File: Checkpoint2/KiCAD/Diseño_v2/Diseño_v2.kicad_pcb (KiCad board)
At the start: 2 copper layers, 160 x 125 mm, 41 parts, among them J1 Conn_01x02, J2 Conn_01x02, J3 Conn_01x03, Q1 BC547, Q2 BC547, Q3 BC557, Q4 BC557, Q5 BC547, Q6 TIP32A, Q7 BC547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

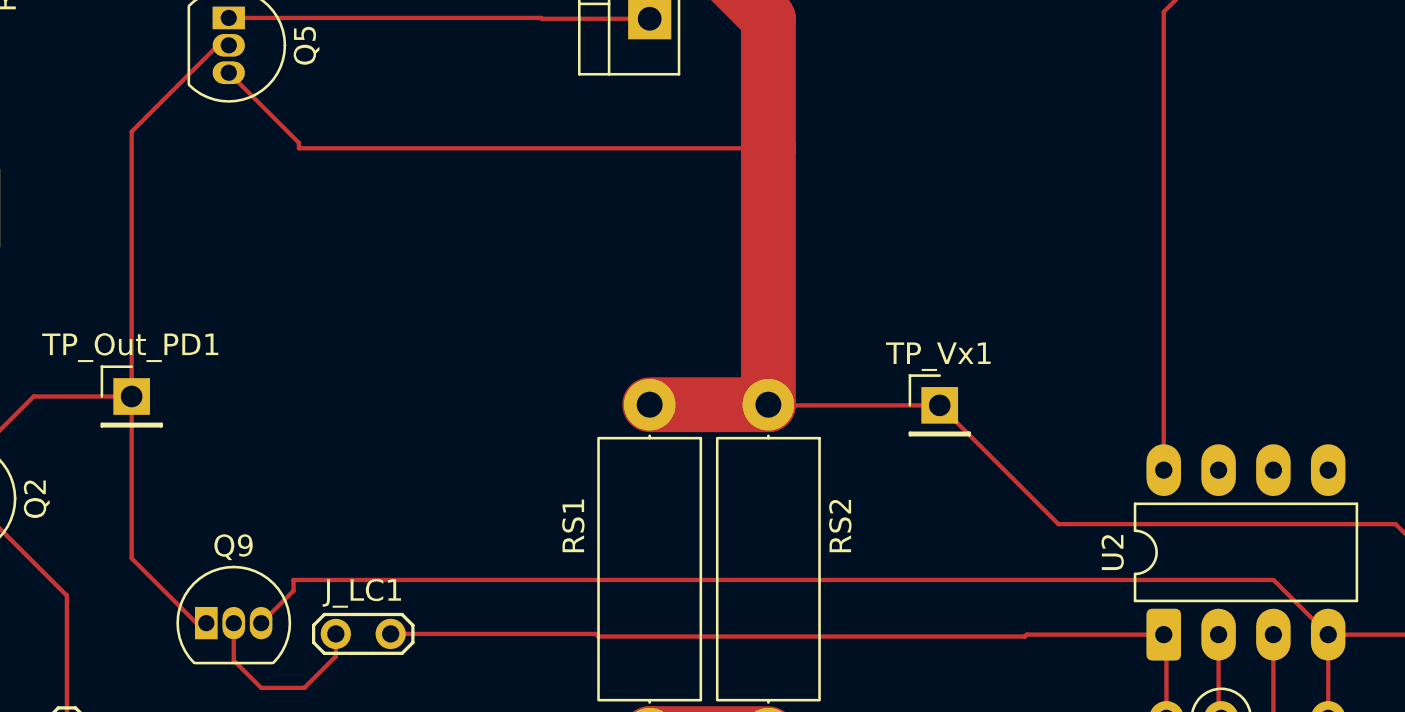
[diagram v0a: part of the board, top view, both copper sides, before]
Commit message: agregué el capacitor de compensación
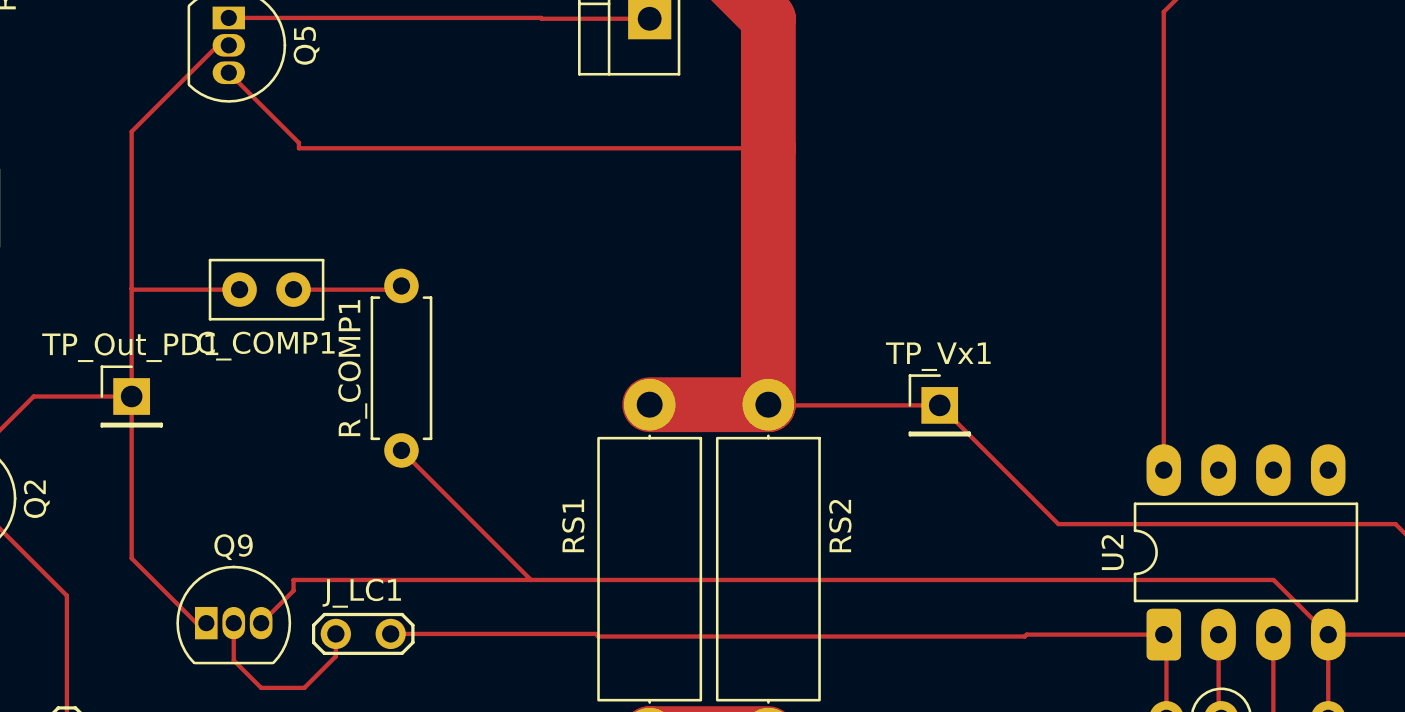
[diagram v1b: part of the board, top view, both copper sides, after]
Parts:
- added C_COMP1: 68n, Capacitor_THT:C_Disc_D5.0mm_W2.5mm_P2.50mm, F.Cu at (141.0, 69.5)
- added R_COMP1: 100, Resistor_THT:R_Axial_DIN0207_L6.3mm_D2.5mm_P7.62mm_Horizontal, F.Cu at (146.0, 77.0)
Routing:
- net GND: track 210.0 -> 218.5 mm
- net Net-(C_COMP1-Pad1): track 0.00 -> 5.07 mm
- net Net-(Q2-C): track 51.0 -> 56.0 mm

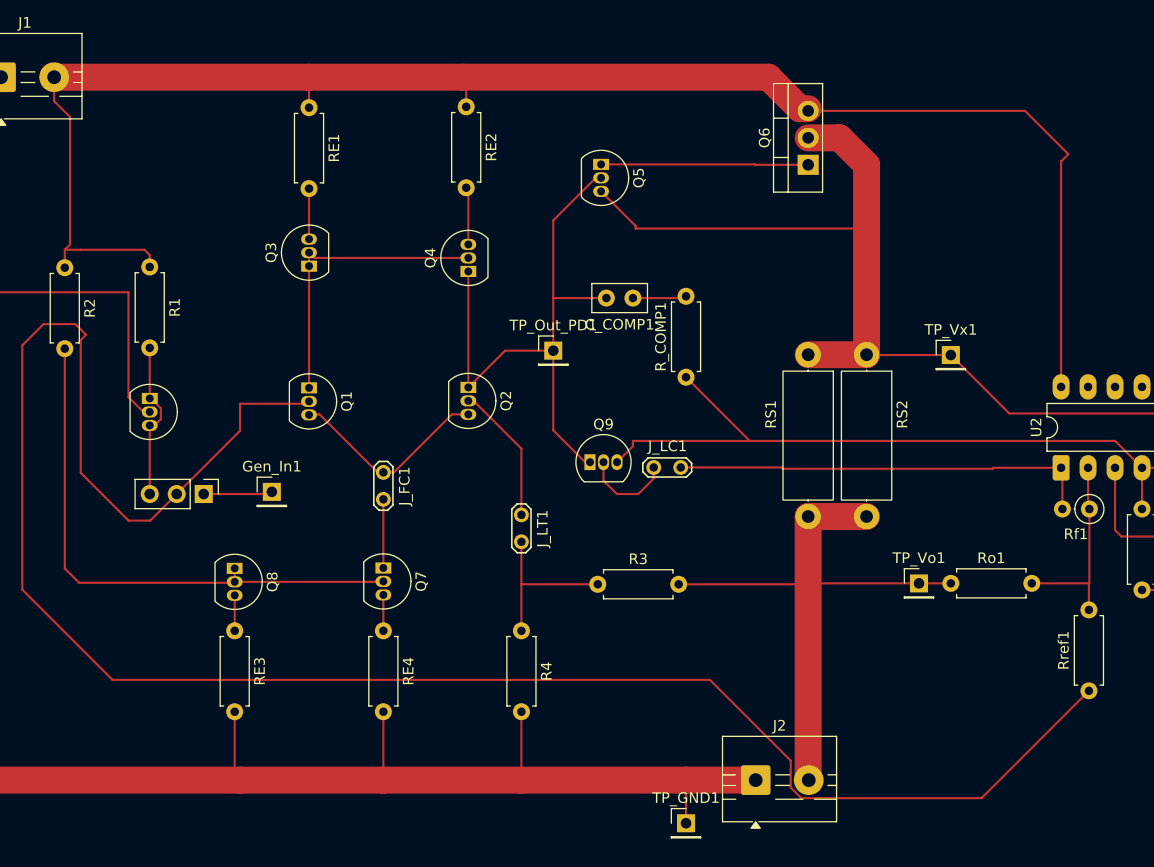
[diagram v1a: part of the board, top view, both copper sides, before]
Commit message: Cambié las huellas de los TBJ xq estaban muy juntas
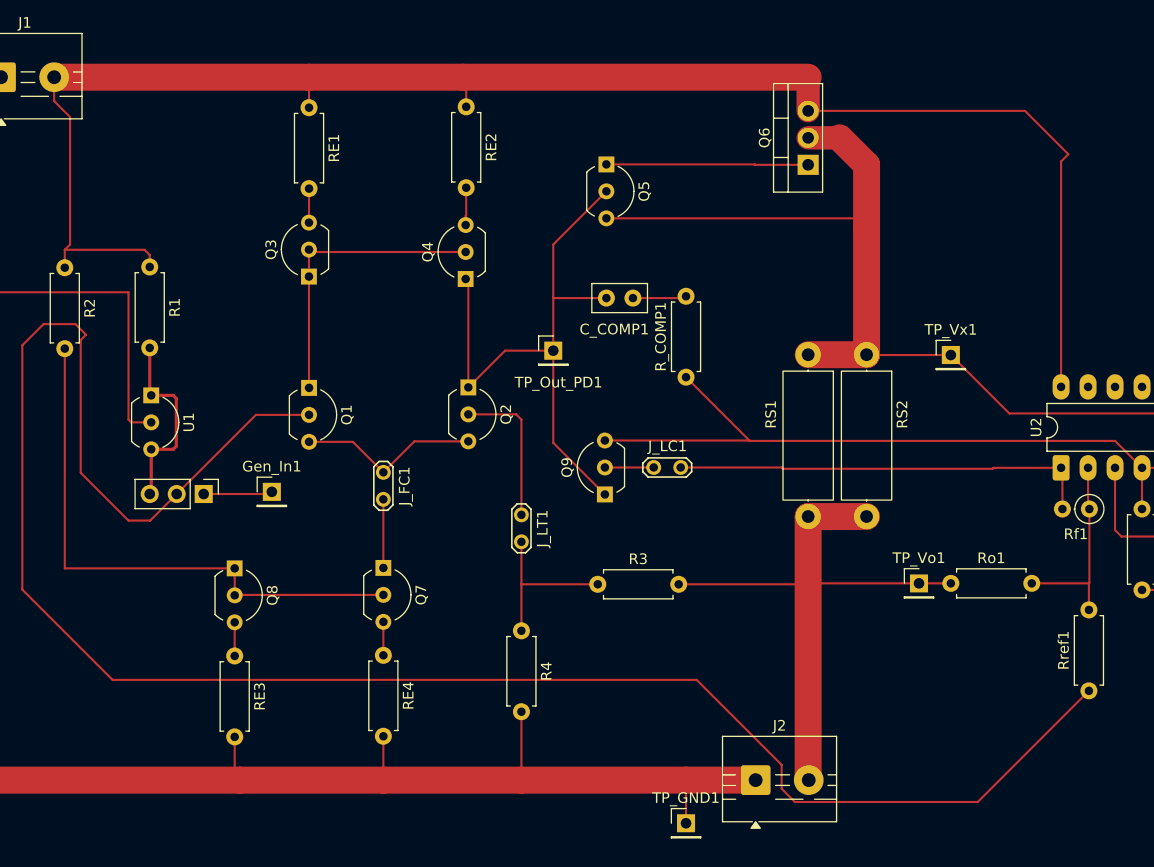
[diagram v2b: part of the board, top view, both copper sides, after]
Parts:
- Q1, Q2, Q3, Q4, Q5, Q7, Q8, Q9, U1: footprint Package_TO_SOT_THT:TO-92_Inline -> Package_TO_SOT_THT:TO-92_Inline_Wide
- moved Q9 3.35 mm to (138.4, 88.0), turned to 90 degrees
- moved RE3 2.37 mm to (103.5, 103.2)
- moved RE4 2.31 mm to (117.5, 103.2)
- moved Q3 0.98 mm to (110.5, 67.5)
- moved Q4 0.75 mm to (125.2, 67.8)
- moved Q5 0.50 mm to (138.5, 57.0)
- moved U1 0.32 mm to (95.6, 78.7)
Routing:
- net Net-(J_LC1-A): track 9.01 -> 4.60 mm
- net Net-(J3-Pin_3): track 15.0 -> 18.3 mm
- net GND: track 218.5 -> 215.6 mm
- net Net-(J_FC1-A): track 19.5 -> 17.4 mm
- net Net-(J1-Pin_2): track 154.5 -> 156.4 mm
- net Net-(Q4-E): track 5.42 -> 3.53 mm
- net /Vref: track 187.2 -> 185.3 mm
- net /Vx: track 90.5 -> 88.8 mm
- net Net-(Q3-E): track 4.76 -> 3.21 mm
- net Net-(Q2-C): track 56.0 -> 57.4 mm
- net Net-(J_LT1-A): track 13.1 -> 14.2 mm
- net Net-(Q7-B): track 52.5 -> 53.2 mm
